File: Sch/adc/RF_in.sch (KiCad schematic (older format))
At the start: 62 parts, among them CN1 SMA, CN2 SMA, J3 JP2, J4 JP2, T1 ETC1-1-13, U1 LTC2292, U2 LP5907_SOT-23, U3 LP5907_SOT-23, U4 NC7SVU04-SC70, U5 NC7SVU04-SC70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

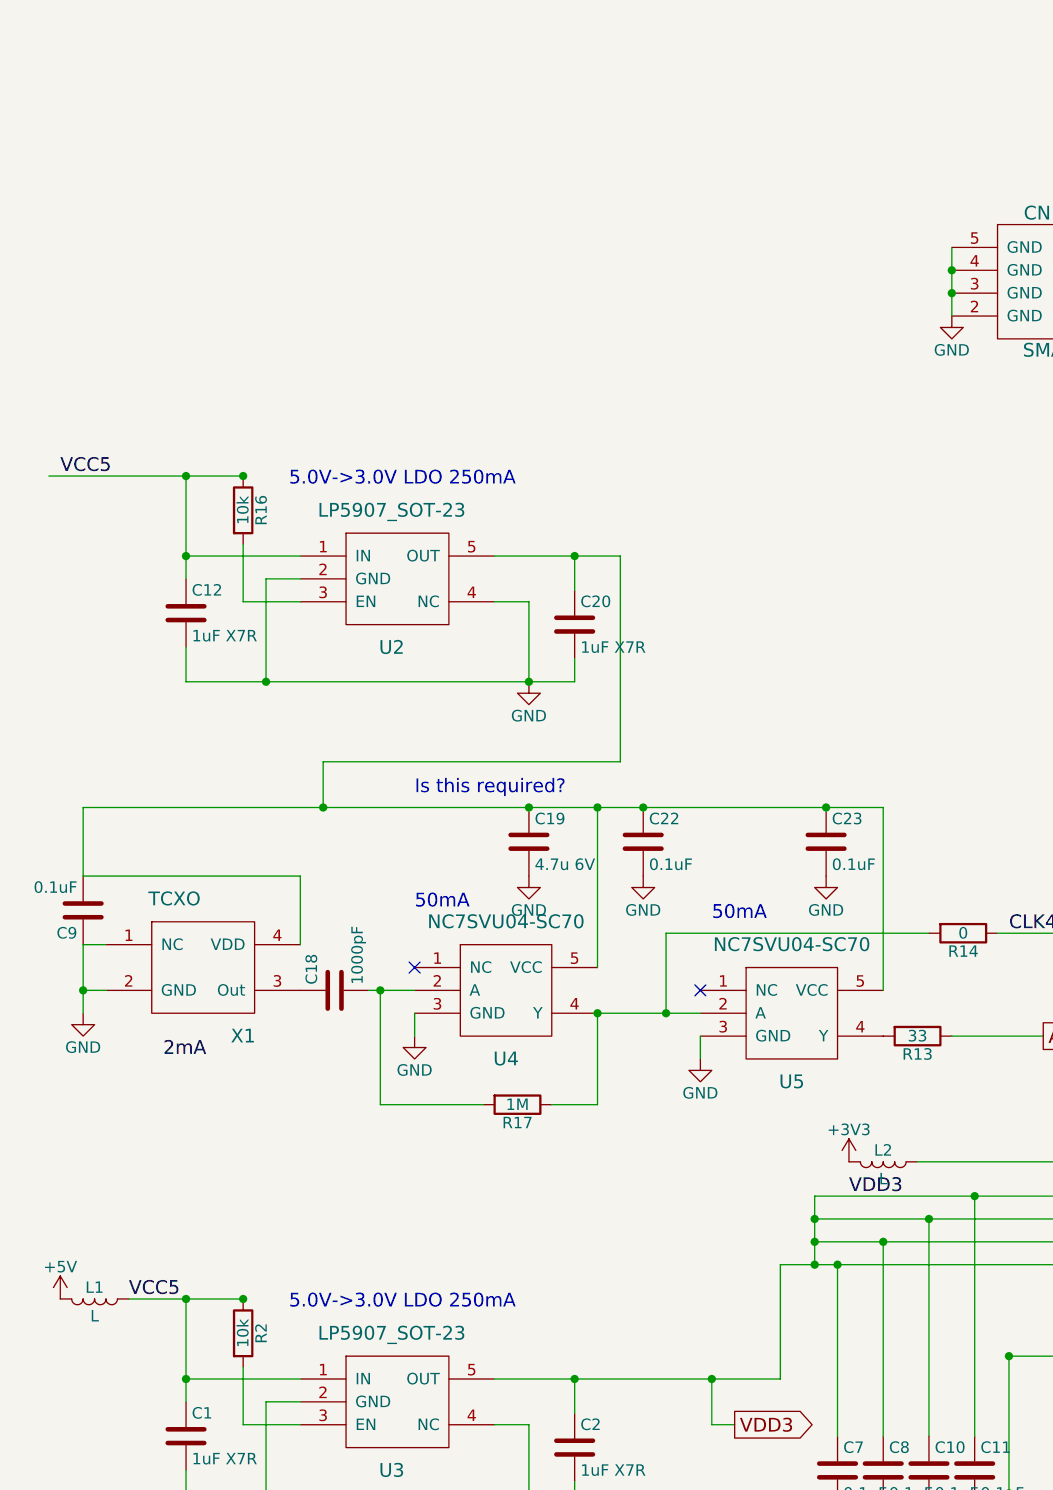
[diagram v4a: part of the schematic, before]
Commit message: Start redesign of ADC board
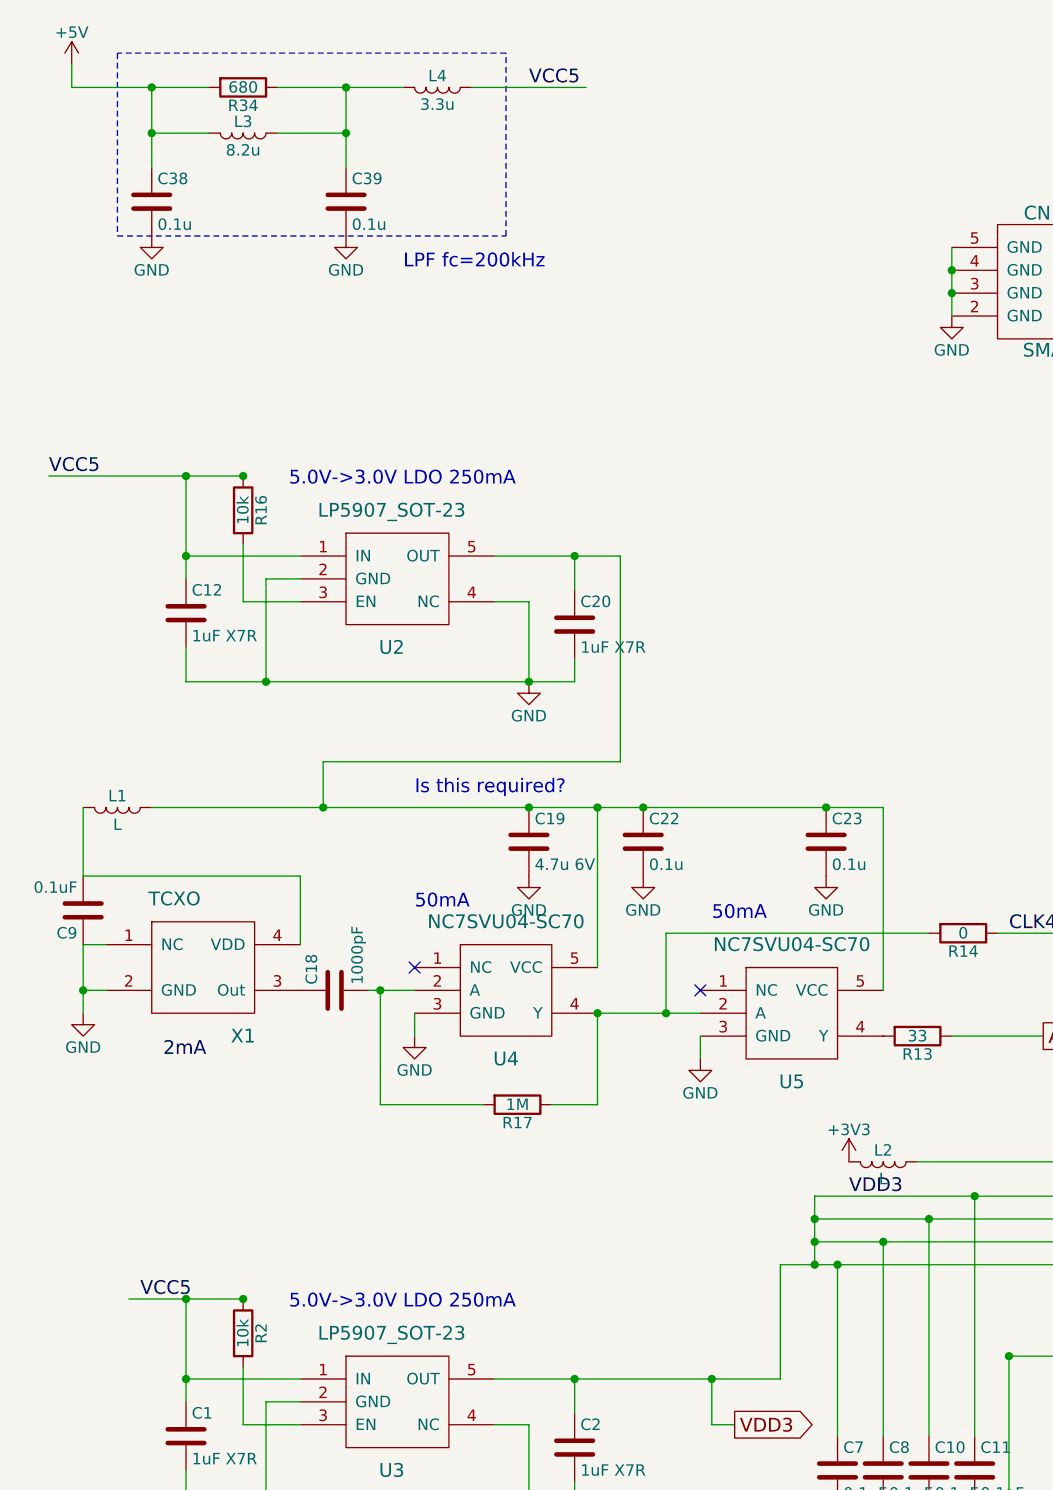
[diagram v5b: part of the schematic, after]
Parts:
- added C38, C39: 0.1u, adc_lib:C0603, symbol C
- added L3: 8.2u, adc_lib:L1008, symbol L
- added L4: 3.3u, adc_lib:L1008, symbol L
- added R34: 680, adc_lib:R0603, symbol R
- C18, C19, C9: footprint adc_lib:C0402 -> adc_lib:C0603
- C22, C23: value 0.1uF -> 0.1u; footprint adc_lib:C0402 -> adc_lib:C0603
- C37: footprint (none) -> adc_lib:C0402
- R17, R20, R33: footprint (none) -> adc_lib:R0603
- R18, R19, R31, R32: footprint (none) -> adc_lib:R0402
- T1: footprint (none) -> adc_lib:ETC1-1-13
- U2, U3: footprint (none) -> adc_lib:LP5907
- U4, U5: footprint (none) -> adc_lib:NC7SVU04-5SC70
- X1: footprint (none) -> adc_lib:TCXO
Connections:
- wire segments 140 -> 148
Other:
- note added: "LPF fc=200kHz"
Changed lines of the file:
@@
 VCMA
-$Comp
-L L L1
-U 1 1 58A5EB01
-P 950 6100
-F 0 "L1" V 900 6100 50  0000 C CNN
-F 1 "L" V 1025 6100 50  0000 C CNN
-F 2 "adc_lib:FB0805" H 950 6100 50  0001 C CNN
-F 3 "" H 950 6100 50  0000 C CNN
-	1    950  6100
-	0    1    1    0
-$EndComp
 $Comp
 L GND #PWR025
@@
 Text Label 4250 5650 0    60   ~ 0
 VDD3
-Text Label 1100 6100 0    60   ~ 0
+Text Label 1150 6100 0    60   ~ 0
 VCC5
 $Comp
@@
 F 0 "X1" H 1600 4350 60  0000 C CNN
 F 1 "TCXO" H 1300 4950 60  0000 C CNN
-F 2 "" H 1600 4350 60  0001 C CNN
+F 2 "adc_lib:TCXO" H 1600 4350 60  0001 C CNN
 F 3 "" H 1600 4350 60  0001 C CNN
 	1    1450 4650
@@
 F 0 "C9" H 925 4500 50  0000 L CNN
 F 1 "0.1uF" H 925 4300 50  0000 L CNN
-F 2 "adc_lib:C0402" H 938 4250 50  0001 C CNN
+F 2 "adc_lib:C0603" H 938 4250 50  0001 C CNN
 F 3 "" H 900 4400 50  0000 C CNN
 	1    900  4400
@@
 F 0 "C18" H 2025 4850 50  0000 L CNN
 F 1 "1000pF" H 2025 4650 50  0000 L CNN
-F 2 "adc_lib:C0402" H 2038 4600 50  0001 C CNN
+F 2 "adc_lib:C0603" H 2038 4600 50  0001 C CNN
 F 3 "" H 2000 4750 50  0000 C CNN
 	1    2000 4750
@@
 F 0 "U4" H 2750 4450 60  0000 C CNN
 F 1 "NC7SVU04-SC70" H 2750 5050 60  0000 C CNN
-F 2 "" H 2750 4450 60  0001 C CNN
+F 2 "adc_lib:NC7SVU04-5SC70" H 2750 4450 60  0001 C CNN
 F 3 "" H 2750 4450 60  0001 C CNN
 	1    2750 4750
@@
 F 0 "R17" V 2880 5250 50  0000 C CNN
 F 1 "1M" V 2800 5250 50  0000 C CNN
-F 2 "" V 2730 5250 50  0000 C CNN
+F 2 "adc_lib:R0603" V 2730 5250 50  0001 C CNN
 F 3 "" H 2800 5250 50  0000 C CNN
 	1    2800 5250
@@
 P 3350 4100
 F 0 "C22" H 3375 4200 50  0000 L CNN
-F 1 "0.1uF" H 3375 4000 50  0000 L CNN
-F 2 "adc_lib:C0402" H 3388 3950 50  0001 C CNN
+F 1 "0.1u" H 3375 4000 50  0000 L CNN
+F 2 "adc_lib:C0603" H 3388 3950 50  0001 C CNN
 F 3 "" H 3350 4100 50  0000 C CNN
 	1    3350 4100
@@
 F 0 "U5" H 4000 4550 60  0000 C CNN
 F 1 "NC7SVU04-SC70" H 4000 5150 60  0000 C CNN
-F 2 "" H 4000 4550 60  0001 C CNN
+F 2 "adc_lib:NC7SVU04-5SC70" H 4000 4550 60  0001 C CNN
 F 3 "" H 4000 4550 60  0001 C CNN
 	1    4000 4850
@@
 P 4150 4100
 F 0 "C23" H 4175 4200 50  0000 L CNN
-F 1 "0.1uF" H 4175 4000 50  0000 L CNN
-F 2 "adc_lib:C0402" H 4188 3950 50  0001 C CNN
+F 1 "0.1u" H 4175 4000 50  0000 L CNN
+F 2 "adc_lib:C0603" H 4188 3950 50  0001 C CNN
 F 3 "" H 4150 4100 50  0000 C CNN
 	1    4150 4100
@@
 F 0 "C19" H 2875 4200 50  0000 L CNN
 F 1 "4.7u 6V" H 2875 4000 50  0000 L CNN
-F 2 "adc_lib:C0402" H 2888 3950 50  0001 C CNN
+F 2 "adc_lib:C0603" H 2888 3950 50  0001 C CNN
 F 3 "" H 2850 4100 50  0000 C CNN
 	1    2850 4100
@@
 F 0 "T1" H 6400 1550 60  0000 C CNN
 F 1 "ETC1-1-13" H 6250 2000 60  0000 C CNN
-F 2 "" H 6400 1550 60  0001 C CNN
+F 2 "adc_lib:ETC1-1-13" H 6400 1550 60  0001 C CNN
 F 3 "" H 6400 1550 60  0001 C CNN
 	1    6250 1750
@@
 F 0 "R18" V 6880 1600 50  0000 C CNN
 F 1 "25" V 6800 1600 50  0000 C CNN
-F 2 "" V 6730 1600 50  0000 C CNN
+F 2 "adc_lib:R0402" V 6730 1600 50  0001 C CNN
 F 3 "" H 6800 1600 50  0000 C CNN
 	1    6800 1600
@@
 F 0 "R19" V 6880 1900 50  0000 C CNN
 F 1 "25" V 6800 1900 50  0000 C CNN
-F 2 "" V 6730 1900 50  0000 C CNN
+F 2 "adc_lib:R0402" V 6730 1900 50  0001 C CNN
 F 3 "" H 6800 1900 50  0000 C CNN
 	1    6800 1900
@@
 F 0 "R32" V 7330 1450 50  0000 C CNN
 F 1 "12" V 7250 1450 50  0000 C CNN
-F 2 "" V 7180 1450 50  0000 C CNN
+F 2 "adc_lib:R0402" V 7180 1450 50  0001 C CNN
 F 3 "" H 7250 1450 50  0000 C CNN
 	1    7250 1450
@@
 F 0 "R31" V 7280 2050 50  0000 C CNN
 F 1 "12" V 7200 2050 50  0000 C CNN
-F 2 "" V 7130 2050 50  0000 C CNN
+F 2 "adc_lib:R0402" V 7130 2050 50  0001 C CNN
 F 3 "" H 7200 2050 50  0000 C CNN
 	1    7200 2050
@@
 F 0 "C37" H 7575 1850 50  0000 L CNN
 F 1 "8p" H 7575 1650 50  0000 L CNN
-F 2 "" H 7588 1600 50  0000 C CNN
+F 2 "adc_lib:C0402" H 7588 1600 50  0001 C CNN
 F 3 "" H 7550 1750 50  0000 C CNN
 	1    7550 1750
@@
 F 0 "R20" V 6930 1300 50  0000 C CNN
 F 1 "0" V 6850 1300 50  0000 C CNN
-F 2 "" V 6780 1300 50  0000 C CNN
+F 2 "adc_lib:R0603" V 6780 1300 50  0001 C CNN
 F 3 "" H 6850 1300 50  0000 C CNN
 	1    6850 1300
@@
 Wire Wire Line
 	2150 4750 2350 4750
-Wire Wire Line
-	900  3950 4400 3950
 Wire Wire Line
 	3150 3950 3150 4650
@@
 F 0 "R33" V 7530 2750 50  0000 C CNN
 F 1 "0" V 7450 2750 50  0000 C CNN
-F 2 "" V 7380 2750 50  0000 C CNN
+F 2 "adc_lib:R0603" V 7380 2750 50  0001 C CNN
 F 3 "" H 7450 2750 50  0000 C CNN
 	1    7450 2750
@@
 F 0 "U3" H 2250 6250 60  0000 C CNN
 F 1 "LP5907_SOT-23" H 2250 6850 60  0000 C CNN
-F 2 "" H 2250 6250 60  0001 C CNN
+F 2 "adc_lib:LP5907" H 2250 6250 60  0001 C CNN
 F 3 "" H 2250 6250 60  0001 C CNN
 	1    2250 6550
@@
 $EndComp
 $Comp
-L +5V #PWR046
-U 1 1 59567851
-P 800 6100
-F 0 "#PWR046" H 800 5950 50  0001 C CNN
-F 1 "+5V" H 800 6240 50  0000 C CNN
-F 2 "" H 800 6100 50  0000 C CNN
-F 3 "" H 800 6100 50  0000 C CNN
-	1    800  6100
-	1    0    0    -1
-$EndComp
-$Comp
-L +3V3 #PWR047
+L +3V3 #PWR046
 U 1 1 5956828F
 P 4250 5500
-F 0 "#PWR047" H 4250 5350 50  0001 C CNN
+F 0 "#PWR046" H 4250 5350 50  0001 C CNN
 F 1 "+3V3" H 4250 5640 50  0000 C CNN
 F 2 "" H 4250 5500 50  0000 C CNN
@@
 	3050 7000 3050 6900
 $Comp
-L GND #PWR048
+L GND #PWR047
 U 1 1 5956A6B3
 P 2850 3400
-F 0 "#PWR048" H 2850 3150 50  0001 C CNN
+F 0 "#PWR047" H 2850 3150 50  0001 C CNN
 F 1 "GND" H 2850 3250 50  0000 C CNN
 F 2 "" H 2850 3400 50  0000 C CNN
@@
 F 0 "U2" H 2250 2650 60  0000 C CNN
 F 1 "LP5907_SOT-23" H 2250 3250 60  0000 C CNN
-F 2 "" H 2250 2650 60  0001 C CNN
+F 2 "adc_lib:LP5907" H 2250 2650 60  0001 C CNN
 F 3 "" H 2250 2650 60  0001 C CNN
 	1    2250 2950
@@
 Text Notes 2350 3900 0    60   ~ 0
 Is this required?
-Text Label 800  2500 0    60   ~ 0
+Text Label 2850 800  0    60   ~ 0
 VCC5
 Text Notes 5750 1350 0    60   ~ 0
 70-170MHz
+$Comp
+L L L3
+U 1 1 598044D7
+P 1600 1000
+F 0 "L3" V 1550 1000 50  0000 C CNN
+F 1 "8.2u" V 1675 1000 50  0000 C CNN
+F 2 "adc_lib:L1008" H 1600 1000 50  0001 C CNN
+F 3 "" H 1600 1000 50  0000 C CNN
+	1    1600 1000
+	0    1    1    0
+$EndComp
+$Comp
+L +5V #PWR048
+U 1 1 598044DD
+P 850 700
+F 0 "#PWR048" H 850 550 50  0001 C CNN
+F 1 "+5V" H 850 840 50  0000 C CNN
+F 2 "" H 850 700 50  0000 C CNN
+F 3 "" H 850 700 50  0000 C CNN
+	1    850  700
+	1    0    0    -1
+$EndComp
+$Comp
+L C C38
+U 1 1 59804643
+P 1200 1300
+F 0 "C38" H 1225 1400 50  0000 L CNN
+F 1 "0.1u" H 1225 1200 50  0000 L CNN
+F 2 "adc_lib:C0603" H 1238 1150 50  0001 C CNN
+F 3 "" H 1200 1300 50  0000 C CNN
+	1    1200 1300
+	1    0    0    -1
+$EndComp
+$Comp
+L GND #PWR049
+U 1 1 598046E8
+P 1200 1450
+F 0 "#PWR049" H 1200 1200 50  0001 C CNN
+F 1 "GND" H 1200 1300 50  0000 C CNN
+F 2 "" H 1200 1450 50  0000 C CNN
+F 3 "" H 1200 1450 50  0000 C CNN
+	1    1200 1450
+	1    0    0    -1
+$EndComp
+$Comp
+L R R34
+U 1 1 5980477E
+P 1600 800
+F 0 "R34" V 1680 800 50  0000 C CNN
+F 1 "680" V 1600 800 50  0000 C CNN
+F 2 "adc_lib:R0603" V 1530 800 50  0001 C CNN
+F 3 "" H 1600 800 50  0000 C CNN
+	1    1600 800
+	0    1    1    0
+$EndComp
+$Comp
+L C C39
+U 1 1 59804ABC
+P 2050 1300
+F 0 "C39" H 2075 1400 50  0000 L CNN
+F 1 "0.1u" H 2075 1200 50  0000 L CNN
+F 2 "adc_lib:C0603" H 2088 1150 50  0001 C CNN
+F 3 "" H 2050 1300 50  0000 C CNN
+	1    2050 1300
+	1    0    0    -1
+$EndComp
+$Comp
+L GND #PWR050
+U 1 1 59804AC2
+P 2050 1450
+F 0 "#PWR050" H 2050 1200 50  0001 C CNN
+F 1 "GND" H 2050 1300 50  0000 C CNN
+F 2 "" H 2050 1450 50  0000 C CNN
+F 3 "" H 2050 1450 50  0000 C CNN
+	1    2050 1450
+	1    0    0    -1
+$EndComp
+$Comp
+L L L4
+U 1 1 59804B77
+P 2450 800
+F 0 "L4" V 2400 800 50  0000 C CNN
+F 1 "3.3u" V 2525 800 50  0000 C CNN
+F 2 "adc_lib:L1008" H 2450 800 50  0001 C CNN
+F 3 "" H 2450 800 50  0000 C CNN
+	1    2450 800
+	0    1    1    0
+$EndComp
+Wire Wire Line
+	850  700  850  800
+Wire Wire Line
+	850  800  1450 800
+Wire Wire Line
+	1200 800  1200 1150
+Connection ~ 1200 800
+Wire Wire Line
+	1200 1000 1450 1000
+Connection ~ 1200 1000
+Wire Wire Line
+	1750 1000 2050 1000
+Wire Wire Line
+	2050 800  2050 1150
+Wire Wire Line
+	1750 800  2300 800
+Connection ~ 2050 1000
+Connection ~ 2050 800
+Wire Wire Line
+	2600 800  3100 800
+Wire Notes Line
+	1050 650  1050 1450
+Wire Notes Line
+	1050 1450 2750 1450
+Wire Notes Line
+	2750 1450 2750 650
+Wire Notes Line
+	2750 650  1050 650
+Text Notes 2300 1600 0    60   ~ 0
+LPF fc=200kHz
+Text Label 750  2500 0    60   ~ 0
+VCC5
+$Comp
+L L L1
+U 1 1 59807774
+P 1050 3950
+F 0 "L1" V 1000 3950 50  0000 C CNN
+F 1 "L" V 1125 3950 50  0000 C CNN
+F 2 "adc_lib:FB0805" H 1050 3950 50  0001 C CNN
+F 3 "" H 1050 3950 50  0000 C CNN
+	1    1050 3950
+	0    1    1    0
+$EndComp
+Wire Wire Line
+	1200 3950 4400 3950
 $EndSCHEMATC
